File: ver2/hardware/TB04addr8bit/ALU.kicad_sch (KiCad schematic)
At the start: 23 parts

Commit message: ver2: ゲートICをgatesシートへ集約しアノテーションを掛け直し
- 分散していた8パッケージ(U1/U2/U5/U25/U35/U36/U37/U51)をgatesシートへ集約
- シートをまたぐ11本をグローバルラベル化(~P4/~P5/~OUT_SEL/~CS_RAM/
  ~OE_ROM/CLK_C/CLK_Z/PC_CNT_EN/~PC_PE/~Ena_RS01/~Enb_RS01)
- U40のP2入力がROM_SELに吸着していたのを修正(RAM_SELが逆条件だった)
- !P5の重複インバータを解消、未使用ゲート入力7本をGNDへ
- ALU入力MUXをinPut→PC、PCカウンタをaddrMUX→PCへ移動
- 全体を再アノテーション(シート順採番)。旧→新の対応は電気的変化なしを確認

Co-Authored-By: Claude Opus 5 <noreply@anthropic.com>
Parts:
- renumbered D42 to D801, D43 to D802, D44 to D803, D45 to D804, D46 to D805, D47 to D806, D48 to D807, D49 to D808, D50 to D809, D51 to D810, D52 to D811, D53 to D812, D54 to D813, D55 to D814, D56 to D815, D57 to D816, D58 to D817, D59 to D818, D60 to D819, D61 to D820, RN6 to RN801, RN7 to RN802, RN8 to RN803
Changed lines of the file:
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@@
 		(dnp no)
 		(fields_autoplaced yes)
-		(property "Reference" "D60"
+		(property "Reference" "D819"
 			(at 237.49 112.0774 90)
 			(show_name no)
@@
 			(project "TB04addr8bit"
 				(path "/d176c79b-dced-4d01-bcec-7dfd676fcfc2/8128481a-591d-4f1a-bdfd-fb80959a87d7"
-					(reference "D60")
+					(reference "D819")
 					(unit 1)
 				)
@@
 		(dnp no)
 		(fields_autoplaced yes)
-		(property "Reference" "D49"
+		(property "Reference" "D808"
 			(at 96.52 105.7274 90)
 			(show_name no)
@@
 			(project "TB04addr8bit"
 				(path "/d176c79b-dced-4d01-bcec-7dfd676fcfc2/8128481a-591d-4f1a-bdfd-fb80959a87d7"
-					(reference "D49")
+					(reference "D808")
 					(unit 1)
 				)
@@
 		(dnp no)
 		(fields_autoplaced yes)
-		(property "Reference" "D45"
+		(property "Reference" "D804"
 			(at 147.32 104.4574 90)
 			(show_name no)
@@
 			(project "TB04addr8bit"
 				(path "/d176c79b-dced-4d01-bcec-7dfd676fcfc2/8128481a-591d-4f1a-bdfd-fb80959a87d7"
-					(reference "D45")
+					(reference "D804")
 					(unit 1)
 				)
@@
 		(dnp no)
 		(fields_autoplaced yes)
-		(property "Reference" "D43"
+		(property "Reference" "D802"
 			(at 330.2 101.9174 90)
 			(show_name no)
@@
 			(project "TB04addr8bit"
 				(path "/d176c79b-dced-4d01-bcec-7dfd676fcfc2/8128481a-591d-4f1a-bdfd-fb80959a87d7"
-					(reference "D43")
+					(reference "D802")
 					(unit 1)
 				)
@@
 		(dnp no)
 		(fields_autoplaced yes)
-		(property "Reference" "D54"
+		(property "Reference" "D813"
 			(at 121.92 110.8074 90)
 			(show_name no)
@@
 			(project "TB04addr8bit"
 				(path "/d176c79b-dced-4d01-bcec-7dfd676fcfc2/8128481a-591d-4f1a-bdfd-fb80959a87d7"
-					(reference "D54")
+					(reference "D813")
 					(unit 1)
 				)
@@
 		(dnp no)
 		(fields_autoplaced yes)
-		(property "Reference" "D47"
+		(property "Reference" "D806"
 			(at 203.2 104.4574 90)
 			(show_name no)
@@
 			(project "TB04addr8bit"
 				(path "/d176c79b-dced-4d01-bcec-7dfd676fcfc2/8128481a-591d-4f1a-bdfd-fb80959a87d7"
-					(reference "D47")
+					(reference "D806")
 					(unit 1)
 				)
@@
 		(dnp no)
 		(fields_autoplaced yes)
-		(property "Reference" "D50"
+		(property "Reference" "D809"
 			(at 246.38 105.7274 90)
 			(show_name no)
@@
 			(project "TB04addr8bit"
 				(path "/d176c79b-dced-4d01-bcec-7dfd676fcfc2/8128481a-591d-4f1a-bdfd-fb80959a87d7"
-					(reference "D50")
+					(reference "D809")
 					(unit 1)
 				)
@@
 		(dnp no)
 		(fields_autoplaced yes)
-		(property "Reference" "RN6"
+		(property "Reference" "RN801"
 			(at 323.85 139.4459 0)
 			(show_name no)
@@
 			(project "TB04addr8bit"
 				(path "/d176c79b-dced-4d01-bcec-7dfd676fcfc2/8128481a-591d-4f1a-bdfd-fb80959a87d7"
-					(reference "RN6")
+					(reference "RN801")
 					(unit 1)
 				)
@@
 		(dnp no)
 		(fields_autoplaced yes)
-		(property "Reference" "D53"
+		(property "Reference" "D812"
 			(at 321.31 108.2674 90)
 			(show_name no)
@@
 			(project "TB04addr8bit"
 				(path "/d176c79b-dced-4d01-bcec-7dfd676fcfc2/8128481a-591d-4f1a-bdfd-fb80959a87d7"
-					(reference "D53")
+					(reference "D812")
 					(unit 1)
 				)
@@
 		(dnp no)
 		(fields_autoplaced yes)
-		(property "Reference" "D42"
+		(property "Reference" "D801"
 			(at 313.69 101.9174 90)
 			(show_name no)
@@
 			(project "TB04addr8bit"
 				(path "/d176c79b-dced-4d01-bcec-7dfd676fcfc2/8128481a-591d-4f1a-bdfd-fb80959a87d7"
-					(reference "D42")
+					(reference "D801")
 					(unit 1)
 				)
@@
 		(dnp no)
 		(fields_autoplaced yes)
-		(property "Reference" "D52"
+		(property "Reference" "D811"
 			(at 304.8 108.2674 90)
 			(show_name no)
@@
 			(project "TB04addr8bit"
 				(path "/d176c79b-dced-4d01-bcec-7dfd676fcfc2/8128481a-591d-4f1a-bdfd-fb80959a87d7"
-					(reference "D52")
+					(reference "D811")
 					(unit 1)
 				)
@@
 		(dnp no)
 		(fields_autoplaced yes)
-		(property "Reference" "RN7"
+		(property "Reference" "RN802"
 			(at 102.87 148.3359 0)
 			(show_name no)
@@
 			(project "TB04addr8bit"
 				(path "/d176c79b-dced-4d01-bcec-7dfd676fcfc2/8128481a-591d-4f1a-bdfd-fb80959a87d7"
-					(reference "RN7")
+					(reference "RN802")
 					(unit 1)
 				)
@@
 		(dnp no)
 		(fields_autoplaced yes)
-		(property "Reference" "D61"
+		(property "Reference" "D820"
 			(at 254 112.0774 90)
 			(show_name no)
@@
 			(project "TB04addr8bit"
 				(path "/d176c79b-dced-4d01-bcec-7dfd676fcfc2/8128481a-591d-4f1a-bdfd-fb80959a87d7"
-					(reference "D61")
+					(reference "D820")
 					(unit 1)
 				)
@@
 		(dnp no)
 		(fields_autoplaced yes)
-		(property "Reference" "RN8"
+		(property "Reference" "RN803"
 			(at 208.28 157.2259 0)
 			(show_name no)
@@
 			(project "TB04addr8bit"
 				(path "/d176c79b-dced-4d01-bcec-7dfd676fcfc2/8128481a-591d-4f1a-bdfd-fb80959a87d7"
-					(reference "RN8")
+					(reference "RN803")
 					(unit 1)
 				)
@@
 		(dnp no)
 		(fields_autoplaced yes)
-		(property "Reference" "D57"
+		(property "Reference" "D816"
 			(at 194.31 110.8074 90)
 			(show_name no)
@@
 			(project "TB04addr8bit"
 				(path "/d176c79b-dced-4d01-bcec-7dfd676fcfc2/8128481a-591d-4f1a-bdfd-fb80959a87d7"
-					(reference "D57")
+					(reference "D816")
 					(unit 1)
 				)
@@
 		(dnp no)
 		(fields_autoplaced yes)
-		(property "Reference" "D58"
+		(property "Reference" "D817"
 			(at 71.12 112.0774 90)
 			(show_name no)
@@
 			(project "TB04addr8bit"
 				(path "/d176c79b-dced-4d01-bcec-7dfd676fcfc2/8128481a-591d-4f1a-bdfd-fb80959a87d7"
-					(reference "D58")
+					(reference "D817")
 					(unit 1)
 				)
@@
 		(dnp no)
 		(fields_autoplaced yes)
-		(property "Reference" "D51"
+		(property "Reference" "D810"
 			(at 262.89 105.7274 90)
 			(show_name no)
@@
 			(project "TB04addr8bit"
 				(path "/d176c79b-dced-4d01-bcec-7dfd676fcfc2/8128481a-591d-4f1a-bdfd-fb80959a87d7"
-					(reference "D51")
+					(reference "D810")
 					(unit 1)
 				)
@@
 		(dnp no)
 		(fields_autoplaced yes)
-		(property "Reference" "D48"
+		(property "Reference" "D807"
 			(at 80.01 105.7274 90)
 			(show_name no)
@@
 			(project "TB04addr8bit"
 				(path "/d176c79b-dced-4d01-bcec-7dfd676fcfc2/8128481a-591d-4f1a-bdfd-fb80959a87d7"
-					(reference "D48")
+					(reference "D807")
 					(unit 1)
 				)
@@
 		(dnp no)
 		(fields_autoplaced yes)
-		(property "Reference" "D44"
+		(property "Reference" "D803"
 			(at 130.81 104.4574 90)
 			(show_name no)
@@
 			(project "TB04addr8bit"
 				(path "/d176c79b-dced-4d01-bcec-7dfd676fcfc2/8128481a-591d-4f1a-bdfd-fb80959a87d7"
-					(reference "D44")
+					(reference "D803")
 					(unit 1)
 				)
@@
 		(dnp no)
 		(fields_autoplaced yes)
-		(property "Reference" "D55"
+		(property "Reference" "D814"
 			(at 138.43 110.8074 90)
 			(show_name no)
@@
 			(project "TB04addr8bit"
 				(path "/d176c79b-dced-4d01-bcec-7dfd676fcfc2/8128481a-591d-4f1a-bdfd-fb80959a87d7"
-					(reference "D55")
+					(reference "D814")
 					(unit 1)
 				)
@@
 		(dnp no)
 		(fields_autoplaced yes)
-		(property "Reference" "#PWR0118"
+		(property "Reference" "#PWR0802"
 			(at 105.41 165.1 0)
 			(hide yes)
@@
 			(project "TB04addr8bit"
 				(path "/d176c79b-dced-4d01-bcec-7dfd676fcfc2/8128481a-591d-4f1a-bdfd-fb80959a87d7"
-					(reference "#PWR0118")
+					(reference "#PWR0802")
 					(unit 1)
 				)
@@
 		(dnp no)
 		(fields_autoplaced yes)
-		(property "Reference" "D59"
+		(property "Reference" "D818"
 			(at 87.63 112.0774 90)
 			(show_name no)
@@
 			(project "TB04addr8bit"
 				(path "/d176c79b-dced-4d01-bcec-7dfd676fcfc2/8128481a-591d-4f1a-bdfd-fb80959a87d7"
-					(reference "D59")
+					(reference "D818")
 					(unit 1)
 				)
@@
 		(dnp no)
 		(fields_autoplaced yes)
-		(property "Reference" "#PWR0117"
+		(property "Reference" "#PWR0801"
 			(at 326.39 154.94 0)
 			(hide yes)
@@
 			(project "TB04addr8bit"
 				(path "/d176c79b-dced-4d01-bcec-7dfd676fcfc2/8128481a-591d-4f1a-bdfd-fb80959a87d7"
-					(reference "#PWR0117")
+					(reference "#PWR0801")
 					(unit 1)
 				)
@@
 		(dnp no)
 		(fields_autoplaced yes)
-		(property "Reference" "D56"
+		(property "Reference" "D815"
 			(at 177.8 110.8074 90)
 			(show_name no)
@@
 			(project "TB04addr8bit"
 				(path "/d176c79b-dced-4d01-bcec-7dfd676fcfc2/8128481a-591d-4f1a-bdfd-fb80959a87d7"
-					(reference "D56")
+					(reference "D815")
 					(unit 1)
 				)
@@
 		(dnp no)
 		(fields_autoplaced yes)
-		(property "Reference" "D46"
+		(property "Reference" "D805"
 			(at 186.69 104.4574 90)
 			(show_name no)
@@
 			(project "TB04addr8bit"
 				(path "/d176c79b-dced-4d01-bcec-7dfd676fcfc2/8128481a-591d-4f1a-bdfd-fb80959a87d7"
-					(reference "D46")
+					(reference "D805")
 					(unit 1)
 				)
@@
 		(dnp no)
 		(fields_autoplaced yes)
-		(property "Reference" "#PWR0119"
+		(property "Reference" "#PWR0803"
 			(at 210.82 172.72 0)
 			(hide yes)
@@
 			(project "TB04addr8bit"
 				(path "/d176c79b-dced-4d01-bcec-7dfd676fcfc2/8128481a-591d-4f1a-bdfd-fb80959a87d7"
-					(reference "#PWR0119")
-					(unit 1)
-				)
+					(reference "#PWR0803")
+					(unit 1)
+				)

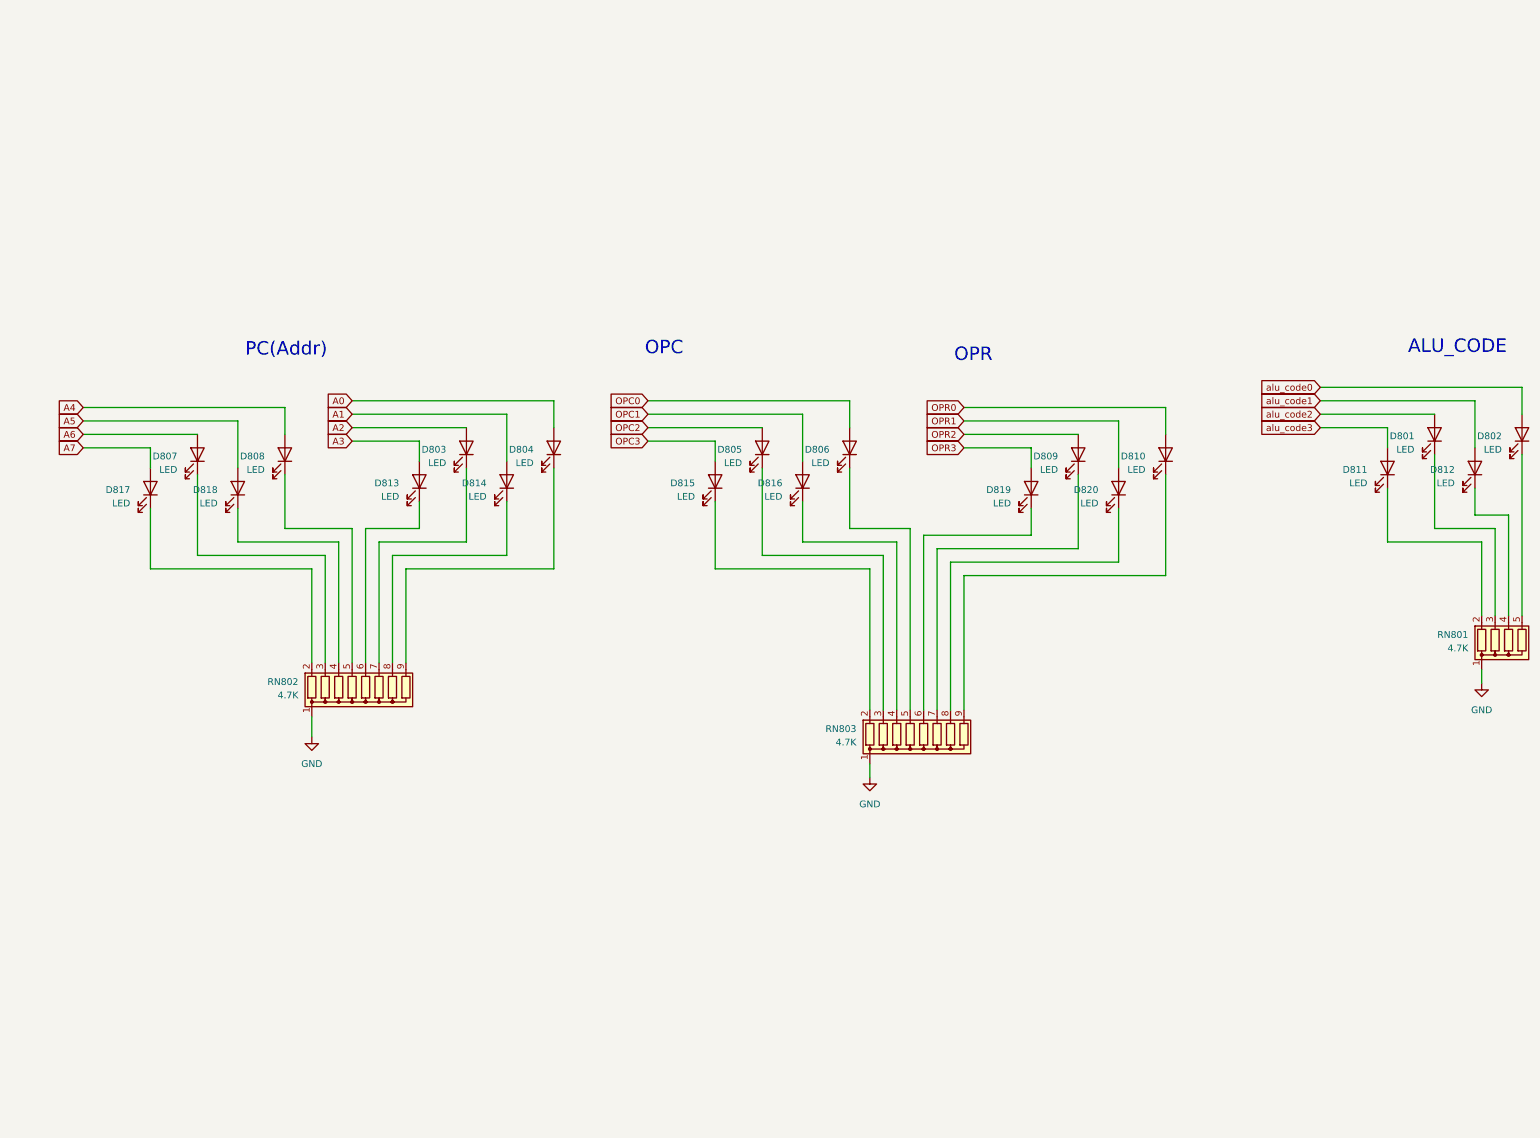
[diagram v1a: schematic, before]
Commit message: ver2: 表示器を2x5コネクタ方式に変更し外付け7segIFで見せる構成に
本体のレジスタLED等を廃止し、7segIF互換の2x5コネクタ21個で外に出す方式へ。
InterFaceシートを新設しOPC/OPR0-11・MD・PC_Qを追加、R0-7とalu_codeも
コネクタ化。SP0-2のLEDを追加。既存部品のネット変更は0件で巻き添えなし。

あわせて命令ROM(U604)にバンク切替スイッチSW601(SW_Coded_SH-7050)を追加し、
A8-A11で256バイト×16バンクを選べるようにした。

要対応: A8-A11にプルダウン(10K)が無く、未選択の接点が開放で浮く。

Co-Authored-By: Claude Opus 5 <noreply@anthropic.com>
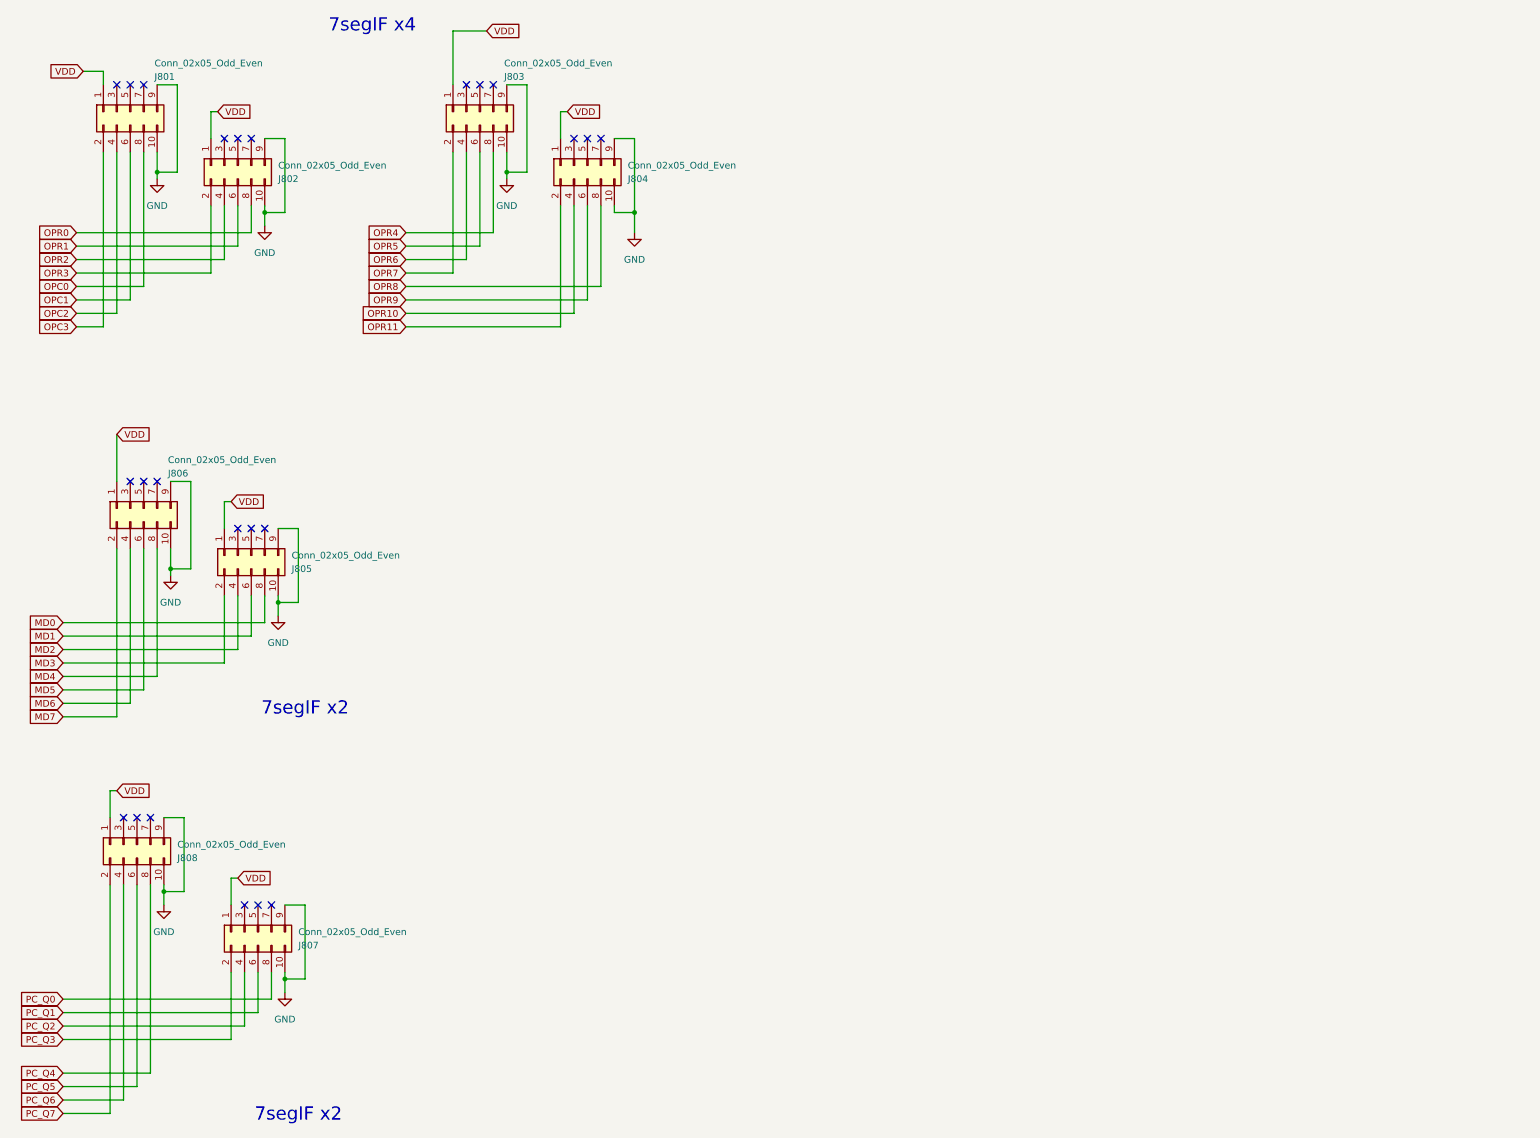
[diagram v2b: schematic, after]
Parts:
- removed D801, D802, D803, D804, D805, D806, D807, D808, D809, D810, D811, D812, D813, D814, D815, D816, D817, D818, D819, D820: LED, LED_THT:LED_D3.0mm_Clear, symbol Device:LED
- removed RN801: 4.7K, Resistor_THT:R_Array_SIP5, symbol Device:R_Network04
- removed RN802, RN803: 4.7K, Resistor_THT:R_Array_SIP9, symbol Device:R_Network08
- added J801, J802, J803, J804, J805, J806, J807, J808: Conn_02x05_Odd_Even, symbol Connector_Generic:Conn_02x05_Odd_Even
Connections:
- net GND: now also J801.10 (Pin_10), J801.9 (Pin_9), J802.10 (Pin_10), J802.9 (Pin_9), J803.10 (Pin_10), J803.9 (Pin_9), J804.10 (Pin_10), J804.9 (Pin_9), J805.10 (Pin_10), J805.9 (Pin_9), J806.10 (Pin_10), J806.9 (Pin_9), J807.10 (Pin_10), J807.9 (Pin_9), J808.10 (Pin_10), J808.9 (Pin_9)
- net OPC0: now also J801.8 (Pin_8)
- net OPC1: now also J801.6 (Pin_6)
- net OPC2: now also J801.4 (Pin_4)
- net OPC3: now also J801.2 (Pin_2)
- net OPR0: now also J802.8 (Pin_8)
- net OPR1: now also J802.6 (Pin_6)
- net OPR2: now also J802.4 (Pin_4)
- net OPR3: now also J802.2 (Pin_2)
- new net MD0: J805.8 (Pin_8)
- new net MD1: J805.6 (Pin_6)
- new net MD2: J805.4 (Pin_4)
- new net MD3: J805.2 (Pin_2)
- new net MD4: J806.8 (Pin_8)
- new net MD5: J806.6 (Pin_6)
- new net MD6: J806.4 (Pin_4)
- new net MD7: J806.2 (Pin_2)
- new net OPR10: J804.4 (Pin_4)
- new net OPR11: J804.2 (Pin_2)
- new net OPR4: J803.8 (Pin_8)
- new net OPR5: J803.6 (Pin_6)
- new net OPR6: J803.4 (Pin_4)
- new net OPR7: J803.2 (Pin_2)
- new net OPR8: J804.8 (Pin_8)
- new net OPR9: J804.6 (Pin_6)
- new net PC_Q0: J807.8 (Pin_8)
- new net PC_Q1: J807.6 (Pin_6)
- new net PC_Q2: J807.4 (Pin_4)
- new net PC_Q3: J807.2 (Pin_2)
- new net PC_Q4: J808.8 (Pin_8)
- new net PC_Q5: J808.6 (Pin_6)
- new net PC_Q6: J808.4 (Pin_4)
- new net PC_Q7: J808.2 (Pin_2)
- new net VDD: J801.1 (Pin_1), J802.1 (Pin_1), J803.1 (Pin_1), J804.1 (Pin_1), J805.1 (Pin_1), J806.1 (Pin_1), J807.1 (Pin_1), J808.1 (Pin_1)
- no-connect marks 0 -> 24
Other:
- note added: "7segIF x2"
- note added: "7segIF x4"
- note removed: "ALU_CODE"
- note removed: "OPC"
- note removed: "OPR"
- note removed: "PC(Addr)"
